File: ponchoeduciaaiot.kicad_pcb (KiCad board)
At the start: 2 copper layers, 87 x 81.2 mm, 42 parts, among them J1 TB_1X3, J2 TB_1X2, J3 TB_1X2, Q1 BC548, Q2 BC548, U1 4N25, U2 LM35, U3 4N25, U4 RELAY, U5 RELAY, U6 RN1810E

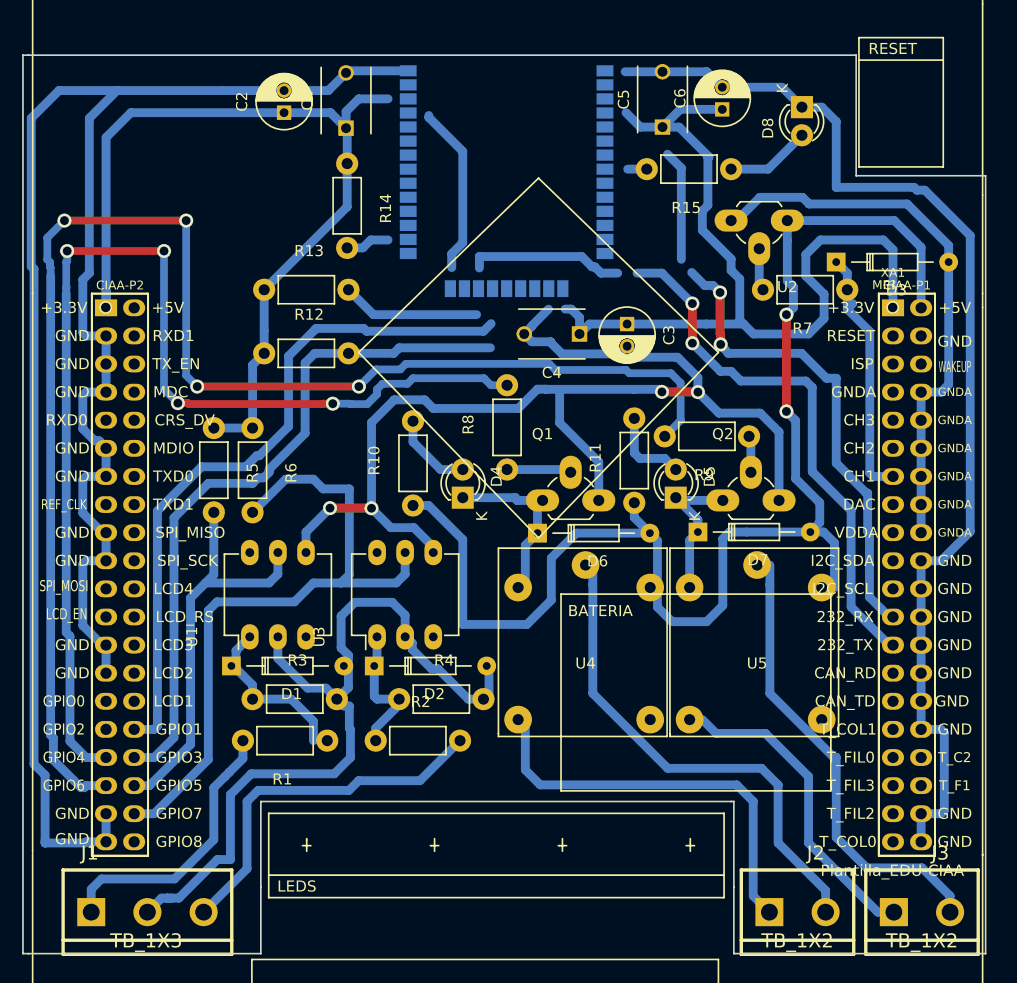
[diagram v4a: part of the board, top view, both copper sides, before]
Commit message: ruteo terminado. reglas OK
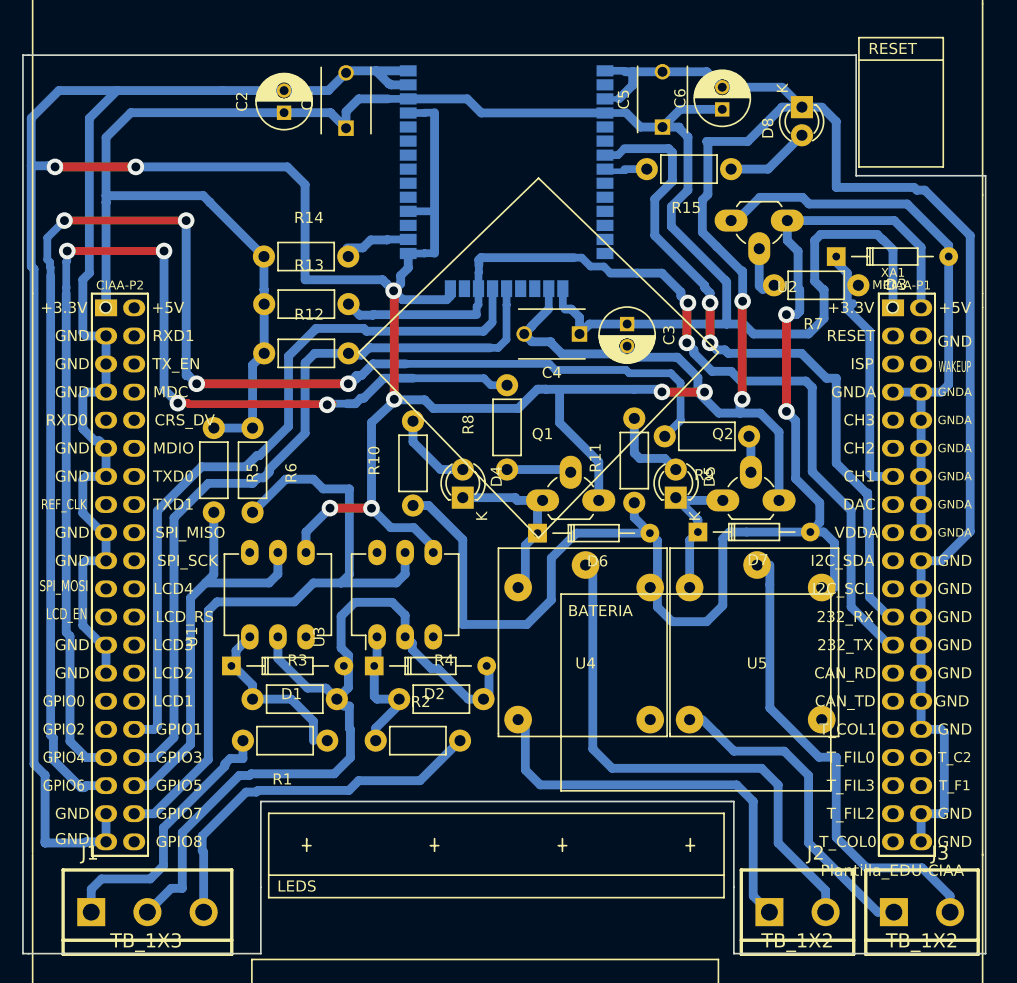
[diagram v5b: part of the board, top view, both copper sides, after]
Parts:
- moved R14 11.3 mm to (110.3, 91.0), turned to 0 degrees
- moved R13 1.30 mm to (110.3, 95.3)
- moved R7 1.08 mm to (164.0, 93.6)
- moved D3 0.50 mm to (162.0, 91.0)
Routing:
- net GND: track 381.8 -> 512.9 mm, vias 4 -> 10
- net (no net): track 39.6 -> 0.00 mm
- net +3V3: track 159.3 -> 185.4 mm
- net /ConectoresPoncho/TXD_EDUCIAA: track 61.4 -> 81.3 mm
- net /ConectoresPoncho/RXD_EDUCIAA: track 43.7 -> 63.1 mm
- net /ConectoresPoncho/MODULE_RESET: track 63.1 -> 69.6 mm
- net Net-(R15-Pad2): track 1.73 -> 5.89 mm
- net /comm/CMD_CTRL: track 63.4 -> 66.6 mm
- net Net-(J2-Pad2): track 45.1 -> 48.0 mm
- net GNDA: track 50.4 -> 52.9 mm
- net Net-(R14-Pad2): track 4.00 -> 5.84 mm
- net Net-(J3-Pad2): track 41.2 -> 42.2 mm
- net +5V: track 123.0 -> 124.0 mm
- net Net-(D1-Pad2): track 73.0 -> 72.0 mm
- net /gpios/OUT1: track 132.6 -> 133.5 mm
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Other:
- net class Default: via_dia 1.27 -> 1.5
- net class INS_BUS added: clearance 0.5, trace_width 0.8, via_dia 1.5, via_drill 0.8
- net class LEDS added: clearance 0.4, trace_width 0.8, via_dia 1.5, via_drill 0.8
- net class MODULE NETS: clearance 0.3 -> 0.2; via_dia 1.27 -> 1.5
- net class OUTS BUS: clearance 0.6 -> 0.5; via_dia 1.27 -> 1.5
- net class PONCHO_CONNECTORS added: clearance 0.4, trace_width 0.8, via_dia 1.5, via_drill 0.8
- rule via_min_size: 1.27 -> 1.5
- board text added: "Grid: 0.2500mm Track with:0.8mm Via:1.5mm / 0.8mm Layers: 1 PCB Surface Finishes: HASL"
- board text removed: "Grid: 0.2500mm Track with:0.8mm Via:1.27mm / 0.8mm Layers: 1 PCB Surface Finishes: HASL"

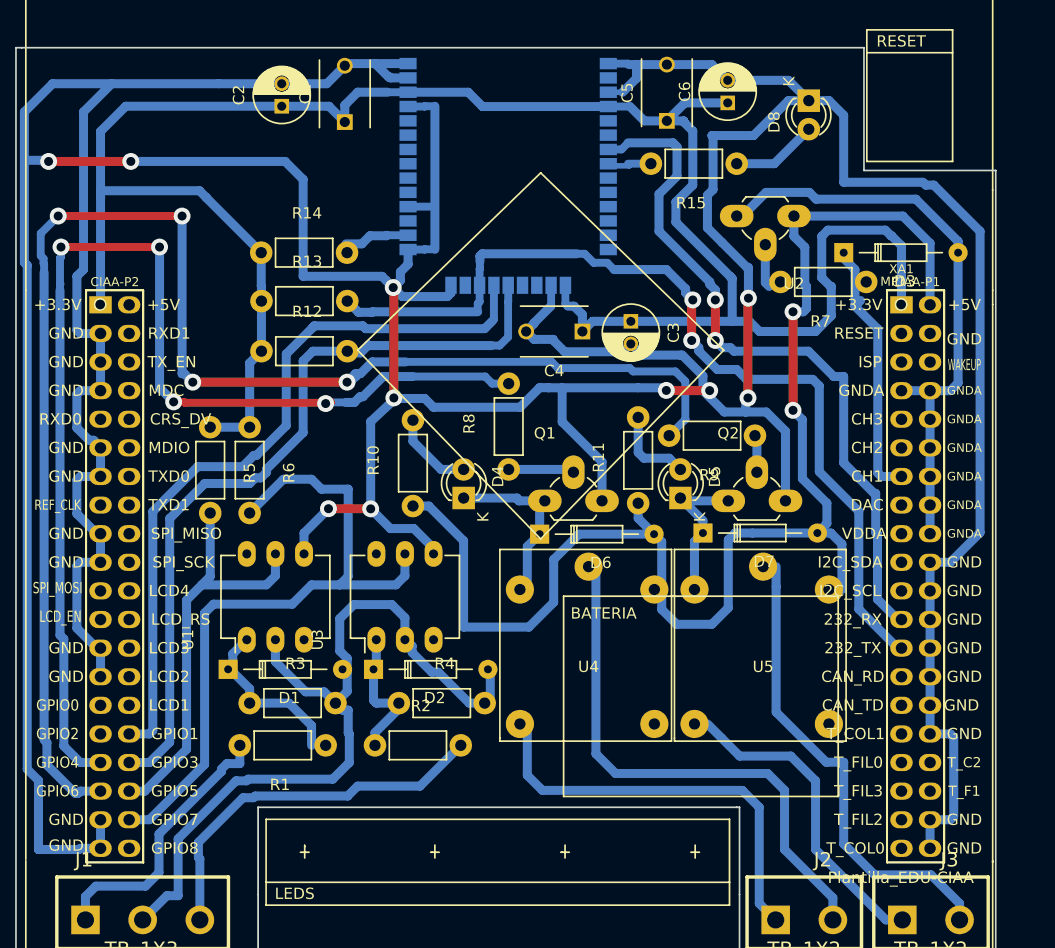
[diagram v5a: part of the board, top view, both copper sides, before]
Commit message: se acomodaron las referencias de los componentes, se pusieron algunos modelos 3d
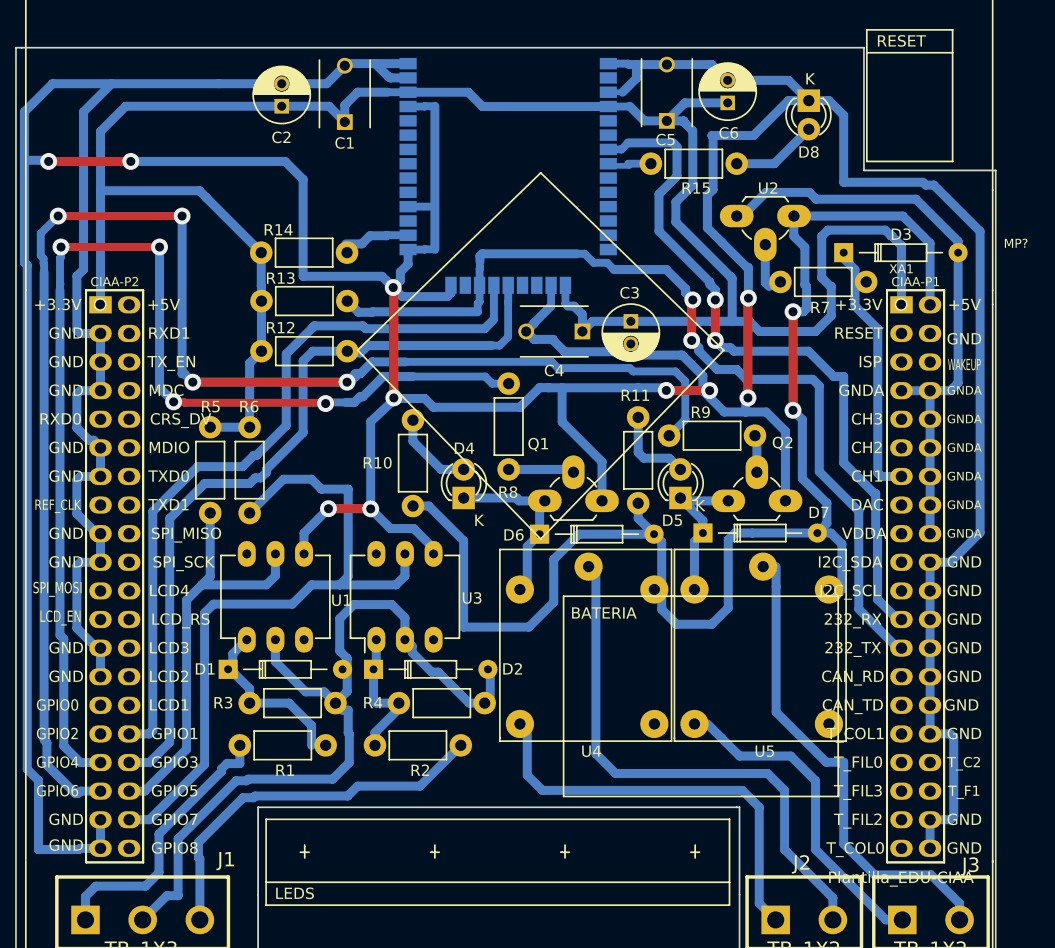
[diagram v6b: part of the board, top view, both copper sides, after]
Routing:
- net /ConectoresPoncho/ANALOG_IN: track 23.3 -> 22.6 mm
